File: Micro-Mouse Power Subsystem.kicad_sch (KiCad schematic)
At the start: 29 parts, among them J1 Pin Header, Q1 2N7002, Q2 AO3401A, Q3 AO3400A, Q4 AO3400A, Q5 AO3401A, U1 TP4056, U2 brushed DC motors, U3 auxiliary motors

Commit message: V1.1
- Refined Motor drivers
- Added USBC
- Added JST (don't know connections yet)
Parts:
- added C9: 1uF, Capacitor_SMD:C_0603_1608Metric, symbol Device:C
- added J2: TYPE-C-31-M-12, Connector_USB:USB_C_Receptacle_HRO_TYPE-C-31-M-12, symbol TYPE-C-31-M-12:TYPE-C-31-M-12
- added J3: Conn_01x02, Connector_JST:JST_PH_B2B-PH-K_1x02_P2.00mm_Vertical, symbol Connector_Generic:Conn_01x02
- added R9: 75K, Resistor_SMD:R_0603_1608Metric, symbol Device:R_US
- added U4: HUSB237-AA001-DN06R, Package_DFN_QFN:DFN-6-1EP_2x2mm_P0.65mm_EP1x1.6mm, symbol custom symbols:HUSB237-AA001-DN06R
- U2, U3: footprint Package_SO:HTSSOP-16-1EP_4.4x5mm_P0.65mm_EP3.4x5mm_Mask3x3mm_ThermalVias -> Package_SO:HTSSOP-16-1EP_4.4x5mm_P0.65mm_EP3.4x5mm_Mask2.46x2.31mm_ThermalVias
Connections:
- net GND: now also C9.2, J2.A1 (GND), J2.A12 (GND), J2.B1 (GND), J2.B12 (GND), J2.S1 (SHIELD), R9.2, U4.7 (GND)
- net HV (9V): now reaches J1.22 (Pin_22)
- net HV (9V): now also C9.1, J2.A4 (VBUS), J2.A9 (VBUS), J2.B4 (VBUS), J2.B9 (VBUS), U4.2 (VBUS)
- new net: J2.A5 (CC1), U4.1 (CC1)
- new net: R9.1, U4.3 (VSET)
- new net: J2.A6 (DP1), J2.B6 (DP2), U4.4 (D+)
- new net: J2.A7 (DN1), J2.B7 (DN2), U4.5 (D-)
- new net: J2.B5 (CC2), U4.6 (CC2)
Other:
- note added: "ON/OFF Switch"
- note added: "USB-C to 9V Power Output"
- note removed: "Note: ASK THE HOMIES HOW THEY GOT R_VALS **DOUBLE CHECK CONNECTIONS WITH HOMIES"
- moved on the sheet: C3, C4, C5, C6, C7, C8, R5, R6, R7, R8, U2, U3

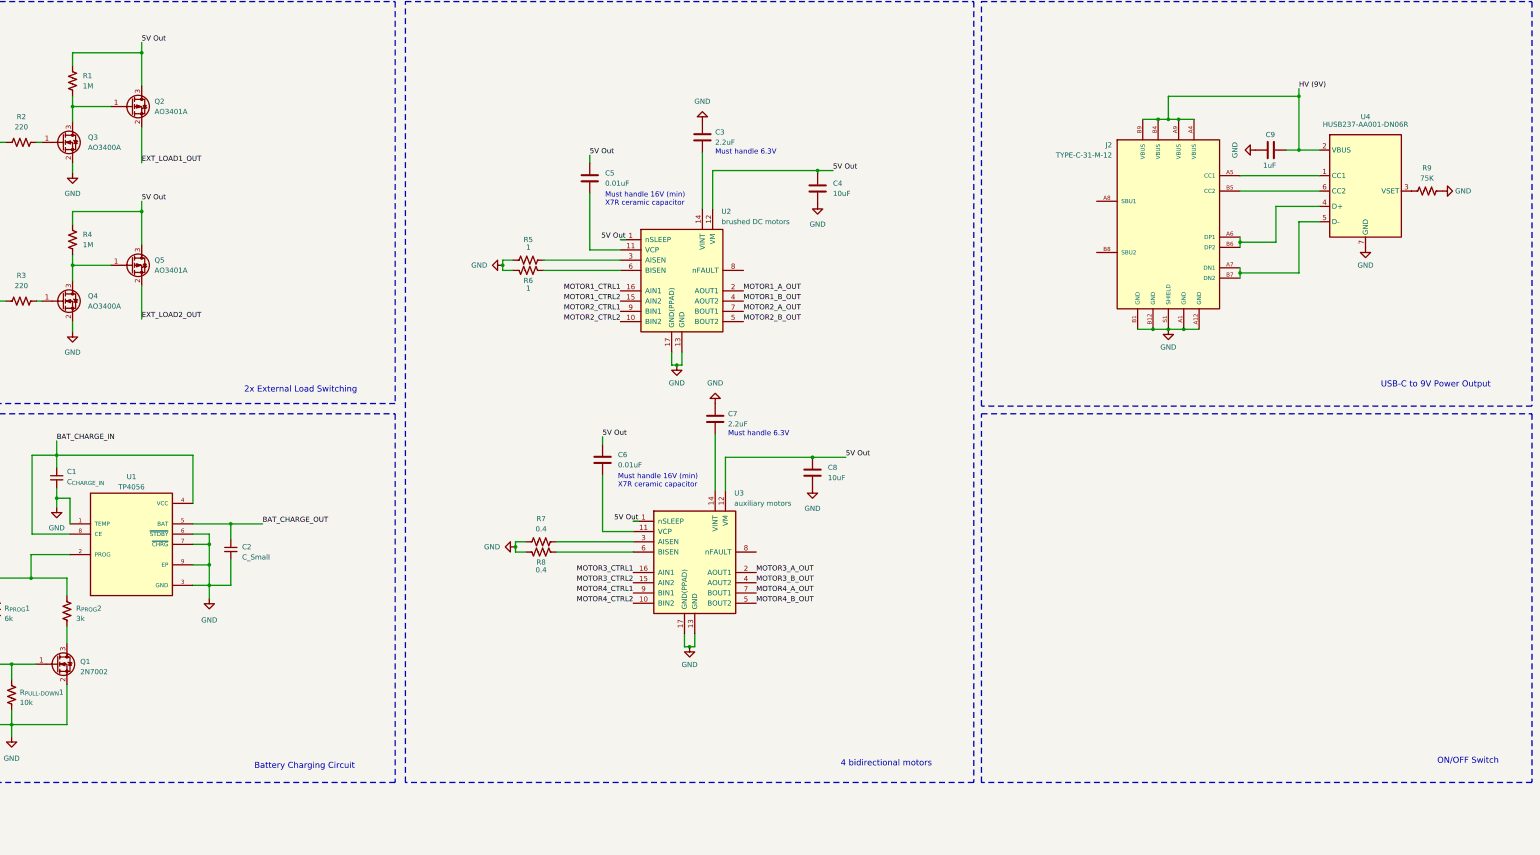
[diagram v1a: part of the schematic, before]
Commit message: still v1.1
-added switch
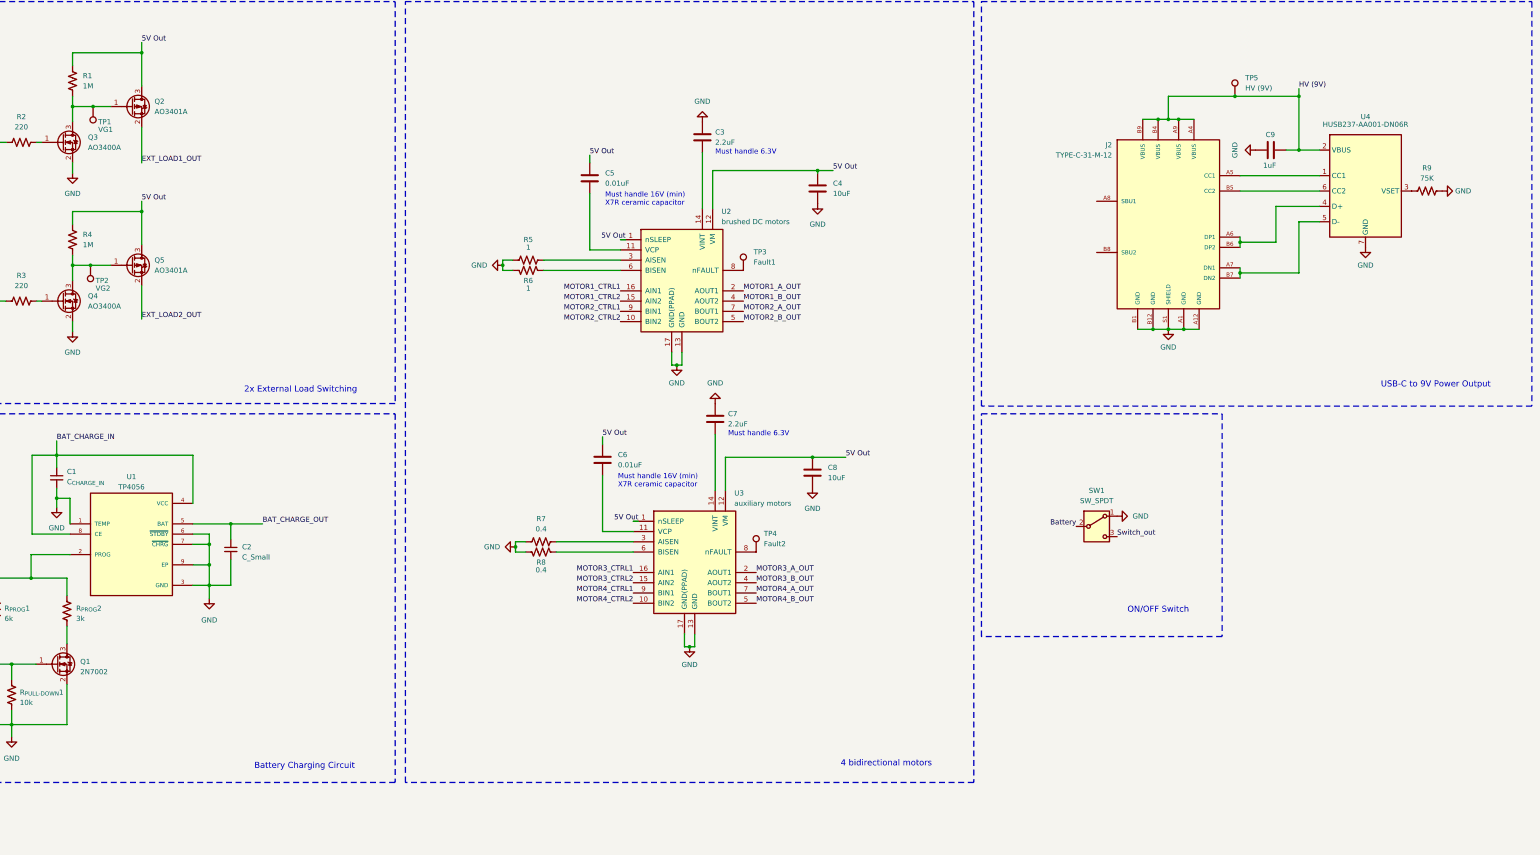
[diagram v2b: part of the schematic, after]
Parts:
- added SW1: SW_SPDT, Connector_Wire:SolderWire-0.75sqmm_1x03_P4.8mm_D1.25mm_OD2.3mm, symbol Switch:SW_SPDT
- added TP1: VG1, symbol Connector:TestPoint
- added TP2: VG2, symbol Connector:TestPoint
- added TP3: Fault1, symbol Connector:TestPoint
- added TP4: Fault2, symbol Connector:TestPoint
- added TP5: HV (9V), symbol Connector:TestPoint
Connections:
- net Battery : now also SW1.2 (B)
- net GND: now also SW1.1 (A)
- net HV (9V): now also TP5.1
- net at Q4.3 (D), Q5.1 (G), R4.2: now also TP2.1
- net at U2.8 (nFAULT): now also TP3.1
- net at U3.8 (nFAULT): now also TP4.1
- net at Q2.1 (G), Q3.3 (D), R1.2: now also TP1.1
- new net Switch_out: SW1.3 (C)
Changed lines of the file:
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@@
   (junction (at 341.63 93.98) (diameter 0) (color 0 0 0 0)
   )
+  (junction (at 78.105 78.105) (diameter 0) (color 0 0 0 0)
+  )
+  (junction (at 78.74 38.735) (diameter 0) (color 0 0 0 0)
+  )
+  (junction (at 361.95 36.195) (diameter 0) (color 0 0 0 0)
+  )
   (junction (at 58.547 177.038) (diameter 0) (color 0 0 0 0)
   )
@@
     (stroke (width 0) (type default))
   )
+  (wire (pts (xy 361.95 36.195) (xy 345.44 36.195))
+    (stroke (width 0) (type default))
+  )
   (wire (pts (xy 64.77 47.625) (xy 66.04 47.625))
     (stroke (width 0) (type default))
@@
     (stroke (width 0) (type default))
   )
+  (wire (pts (xy 78.74 38.735) (xy 83.185 38.735))
+    (stroke (width 0) (type default))
+  )
   (wire (pts (xy 53.975 47.625) (xy 57.15 47.625))
     (stroke (width 0) (type default))
@@
     (stroke (width 0) (type default))
   )
-  (wire (pts (xy 377.825 36.195) (xy 345.44 36.195))
+  (wire (pts (xy 377.825 36.195) (xy 361.95 36.195))
     (stroke (width 0) (type default))
   )
@@
     (stroke (width 0) (type default))
   )
+  (wire (pts (xy 78.105 78.105) (xy 83.185 78.105))
+    (stroke (width 0) (type default))
+  )
   (wire (pts (xy 363.22 80.01) (xy 363.22 81.28))
     (stroke (width 0) (type default))
@@
     (stroke (width 0) (type default))
   )
-  (wire (pts (xy 73.66 78.105) (xy 83.185 78.105))
+  (wire (pts (xy 73.66 78.105) (xy 78.105 78.105))
     (stroke (width 0) (type default))
   )
@@
     (stroke (width 0) (type default))
   )
-  (wire (pts (xy 73.66 38.735) (xy 83.185 38.735))
+  (wire (pts (xy 73.66 38.735) (xy 78.74 38.735))
     (stroke (width 0) (type default))
   )
@@
     (fill (type none))
   )
-  (rectangle (start 299.085 114.935) (end 435.61 206.375)
+  (rectangle (start 299.085 114.935) (end 358.775 170.18)
     (stroke (width 0) (type dash) (color 0 0 0 1))
     (fill (type none))
@@
     (effects (font (size 1.5 1.5) (color 0 0 0 1)) (justify left bottom))
   )
-  (text "ON/OFF Switch" (at 412.115 201.93 0)
+  (text "ON/OFF Switch" (at 335.28 164.465 0)
     (effects (font (size 1.5 1.5) (color 0 0 0 1)) (justify left bottom))
   )
@@
     (effects (font (size 1.27 1.27)) (justify right bottom))
   )
+  (label "Battery " (at 322.58 142.875 180) (fields_autoplaced)
+    (effects (font (size 1.27 1.27)) (justify right bottom))
+  )
   (label "MOTOR1_CTRL1" (at 55.245 382.905 0) (fields_autoplaced)
     (effects (font (size 1.27 1.27)) (justify left bottom))
@@
   )
   (label "3V3 Out " (at 55.245 370.205 0) (fields_autoplaced)
+    (effects (font (size 1.27 1.27)) (justify left bottom))
+  )
+  (label "Switch_out" (at 332.74 145.415 0) (fields_autoplaced)
     (effects (font (size 1.27 1.27)) (justify left bottom))
   )
@@
     )
   )
+  (symbol (lib_id "Connector:TestPoint") (at 361.95 36.195 0) (unit 1)
+    (in_bom yes) (on_board yes) (dnp no) (fields_autoplaced)
+    (property "Reference" "TP5" (at 364.49 31.623 0)
+      (effects (font (size 1.27 1.27)) (justify left))
+    )
+    (property "Value" "HV (9V)" (at 364.49 34.163 0)
+      (effects (font (size 1.27 1.27)) (justify left))
+    )
+    (property "Footprint" "" (at 367.03 36.195 0)
+      (effects (font (size 1.27 1.27)) hide)
+    )
+    (property "Datasheet" "~" (at 367.03 36.195 0)
+      (effects (font (size 1.27 1.27)) hide)
+    )
+    (pin "1")
+    (instances
+      (project "Micro-Mouse Power Subsystem"
+        (path "/b84c8230-4cbd-48ad-931b-8b6e428e7801"
+          (reference "TP5") (unit 1)
+        )
+      )
+    )
+  )
   (symbol (lib_id "Device:R_US") (at 409.575 59.69 90) (unit 1)
     (in_bom yes) (on_board yes) (dnp no) (fields_autoplaced)
@@
         (path "/b84c8230-4cbd-48ad-931b-8b6e428e7801"
           (reference "C4") (unit 1)
+        )
+      )
+    )
+  )
+  (symbol (lib_id "Connector:TestPoint") (at 240.03 79.375 0) (unit 1)
+    (in_bom yes) (on_board yes) (dnp no) (fields_autoplaced)
+    (property "Reference" "TP3" (at 242.57 74.803 0)
+      (effects (font (size 1.27 1.27)) (justify left))
+    )
+    (property "Value" "Fault1" (at 242.57 77.343 0)
+      (effects (font (size 1.27 1.27)) (justify left))
+    )
+    (property "Footprint" "" (at 245.11 79.375 0)
+      (effects (font (size 1.27 1.27)) hide)
+    )
+    (property "Datasheet" "~" (at 245.11 79.375 0)
+      (effects (font (size 1.27 1.27)) hide)
+    )
+    (pin "1")
+    (instances
+      (project "Micro-Mouse Power Subsystem"
+        (path "/b84c8230-4cbd-48ad-931b-8b6e428e7801"
+          (reference "TP3") (unit 1)
         )
       )
@@
     )
   )
+  (symbol (lib_id "Connector:TestPoint") (at 243.205 149.225 0) (unit 1)
+    (in_bom yes) (on_board yes) (dnp no) (fields_autoplaced)
+    (property "Reference" "TP4" (at 245.11 144.653 0)
+      (effects (font (size 1.27 1.27)) (justify left))
+    )
+    (property "Value" "Fault2" (at 245.11 147.193 0)
+      (effects (font (size 1.27 1.27)) (justify left))
+    )
+    (property "Footprint" "" (at 248.285 149.225 0)
+      (effects (font (size 1.27 1.27)) hide)
+    )
+    (property "Datasheet" "~" (at 248.285 149.225 0)
+      (effects (font (size 1.27 1.27)) hide)
+    )
+    (pin "1")
+    (instances
+      (project "Micro-Mouse Power Subsystem"
+        (path "/b84c8230-4cbd-48ad-931b-8b6e428e7801"
+          (reference "TP4") (unit 1)
+        )
+      )
+    )
+  )
+  (symbol (lib_id "Connector:TestPoint") (at 78.74 38.735 0) (mirror x) (unit 1)
+    (in_bom yes) (on_board yes) (dnp no)
+    (property "Reference" "TP1" (at 80.01 42.545 0)
+      (effects (font (size 1.27 1.27)) (justify left))
+    )
+    (property "Value" "VG1" (at 80.01 44.45 0)
+      (effects (font (size 1.27 1.27)) (justify left))
+    )
+    (property "Footprint" "" (at 83.82 38.735 0)
+      (effects (font (size 1.27 1.27)) hide)
+    )
+    (property "Datasheet" "~" (at 83.82 38.735 0)
+      (effects (font (size 1.27 1.27)) hide)
+    )
+    (pin "1")
+    (instances
+      (project "Micro-Mouse Power Subsystem"
+        (path "/b84c8230-4cbd-48ad-931b-8b6e428e7801"
+          (reference "TP1") (unit 1)
+        )
+      )
+    )
+  )
   (symbol (lib_id "power:GND") (at 58.547 195.072 0) (unit 1)
     (in_bom yes) (on_board yes) (dnp no) (fields_autoplaced)
@@
         (path "/b84c8230-4cbd-48ad-931b-8b6e428e7801"
           (reference "#PWR010") (unit 1)
+        )
+      )
+    )
+  )
+  (symbol (lib_id "Switch:SW_SPDT") (at 327.66 142.875 0) (unit 1)
+    (in_bom yes) (on_board yes) (dnp no) (fields_autoplaced)
+    (property "Reference" "SW1" (at 327.66 133.985 0)
+      (effects (font (size 1.27 1.27)))
+    )
+    (property "Value" "SW_SPDT" (at 327.66 136.525 0)
+      (effects (font (size 1.27 1.27)))
+    )
+    (property "Footprint" "Connector_Wire:SolderWire-0.75sqmm_1x03_P4.8mm_D1.25mm_OD2.3mm" (at 327.66 142.875 0)
+      (effects (font (size 1.27 1.27)) hide)
+    )
+    (property "Datasheet" "~" (at 327.66 150.495 0)
+      (effects (font (size 1.27 1.27)) hide)
+    )
+    (pin "2")
+    (pin "3")
+    (pin "1")
+    (instances
+      (project "Micro-Mouse Power Subsystem"
+        (path "/b84c8230-4cbd-48ad-931b-8b6e428e7801"
+          (reference "SW1") (unit 1)
         )
       )
@@
     )
   )
+  (symbol (lib_id "power:GND") (at 332.74 140.335 90) (unit 1)
+    (in_bom yes) (on_board yes) (dnp no) (fields_autoplaced)
+    (property "Reference" "#PWR018" (at 339.09 140.335 0)
+      (effects (font (size 1.27 1.27)) hide)
+    )
+    (property "Value" "GND" (at 336.55 140.335 90)
+      (effects (font (size 1.27 1.27)) (justify right))
+    )
+    (property "Footprint" "" (at 332.74 140.335 0)
+      (effects (font (size 1.27 1.27)) hide)
+    )
+    (property "Datasheet" "" (at 332.74 140.335 0)
+      (effects (font (size 1.27 1.27)) hide)
+    )
+    (pin "1")
+    (instances
+      (project "Micro-Mouse Power Subsystem"
+        (path "/b84c8230-4cbd-48ad-931b-8b6e428e7801"
+          (reference "#PWR018") (unit 1)
+        )
+      )
+    )
+  )
   (symbol (lib_id "Connector_Generic:Conn_01x02") (at 132.715 366.395 0) (unit 1)
     (in_bom yes) (on_board yes) (dnp no) (fields_autoplaced)
@@
         )
       )
+    )
+  )
+  (symbol (lib_id "Connector:TestPoint") (at 78.105 78.105 0) (mirror x) (unit 1)
+    (in_bom yes) (on_board yes) (dnp no)
+    (property "Reference" "TP2" (at 79.375 81.915 0)
+      (effects (font (size 1.27 1.27)) (justify left))
+    )
+    (property "Value" "VG2" (at 79.375 83.82 0)
+      (effects (font (size 1.27 1.27)) (justify left))
+    )
+    (property "Footprint" "" (at 83.185 78.105 0)
+      (effects (font (size 1.27 1.27)) hide)
+    )
+    (property "Datasheet" "~" (at 83.185 78.105 0)
+      (effects (font (size 1.27 1.27)) hide)
+    )
+    (pin "1")
+    (instances
+      (project "Micro-Mouse Power Subsystem"
+        (path "/b84c8230-4cbd-48ad-931b-8b6e428e7801"
+          (reference "TP2") (unit 1)
+        )
+      )

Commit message: changes
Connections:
- net GND: no longer SW1.1 (A)
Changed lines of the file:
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@@
-    )
-  )
-  (symbol (lib_id "power:GND") (at 332.74 140.335 90) (unit 1)
-    (in_bom yes) (on_board yes) (dnp no) (fields_autoplaced)
-    (property "Reference" "#PWR018" (at 339.09 140.335 0)
-      (effects (font (size 1.27 1.27)) hide)
-    )
-    (property "Value" "GND" (at 336.55 140.335 90)
-      (effects (font (size 1.27 1.27)) (justify right))
-    )
-    (property "Footprint" "" (at 332.74 140.335 0)
-      (effects (font (size 1.27 1.27)) hide)
-    )
-    (property "Datasheet" "" (at 332.74 140.335 0)
-      (effects (font (size 1.27 1.27)) hide)
-    )
-    (pin "1")
-    (instances
-      (project "Micro-Mouse Power Subsystem"
-        (path "/b84c8230-4cbd-48ad-931b-8b6e428e7801"
-          (reference "#PWR018") (unit 1)
-        )
-      )
     )
   )

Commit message: Update to KiCad 9.0
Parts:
- J3: footprint Connector_JST:JST_PH_B2B-PH-K_1x02_P2.00mm_Vertical -> Connector_JST:JST_PH_S2B-PH-K_1x02_P2.00mm_Horizontal
- TP1, TP2, TP3, TP4, TP5: footprint (none) -> TestPoint:TestPoint_Pad_1.5x1.5mm
- U2: value brushed DC motors -> brushed DC motors
- U3: value auxiliary motors -> auxiliary motors

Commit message: V2
- all schematics are uploaded
- missing a few footprints from Sinaye
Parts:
- removed C1: C_{CHARGE_IN}, Capacitor_SMD:C_0603_1608Metric, symbol Device:C_Small
- removed C2: C_Small, Capacitor_SMD:C_0603_1608Metric, symbol Device:C_Small
- removed R_{PULL-DOWN}1: 10k, Resistor_SMD:R_0603_1608Metric, symbol Device:R_US
- removed U1: TP4056, TP4056:SOP127P600X175-9N, symbol TP4056:TP4056
- added C10, C_{1}1: 1uF, symbol Device:C_Small
- added C_{BOOT}1, C_{BY}1: 0.1uF, symbol Device:C_Small
- added C_{BYPASS}1: 0.1u, symbol Device:C_Small
- added C_{CHARGE_IN}1, C_{CHARGE_OUT}1: 10u, symbol Device:C_Small
- added C_{COMP}1: 1nF, symbol Device:C_Small
- added C_{IN_3.3}1, C_{IN_3.3}2, C_{IN}1, C_{IN}2, C_{OUT_3.3}1, C_{OUT_3.3}2, C_{OUT_3.3}3, C_{OUT}1, C_{OUT}2, C_{OUT}3: 100uF, symbol Device:C_Small
- added C_{IN_3.3}3, C_{IN}3, C_{OUT}4, C_{OUT}5, C_{OUT}6: 22uF, symbol Device:C_Small
- added C_{IN_5}1: 10uF, symbol Device:C_Small
- added C_{SS}1: 47nF, symbol Device:C_Small
- added D3, D4: SK32WA, symbol Device:D_Schottky
- added L1: L, symbol Device:L
- added L2, L4: 22uH, symbol Device:L
- added R_{COMP}1: 68k, symbol Device:R_US
- added R_{FB}1: 150k, symbol Device:R_US
- added R_{FB}2: 47k, symbol Device:R_US
- added R_{FSW}1: 220k, symbol Device:R_US
- added R_{FSW}2: 33k, symbol Device:R_US
- added R_{ILIM}1: 100k, symbol Device:R_US
- added R_{PULL_DOWN}1: 10k, symbol Device:R_US
- added R_{SCL}1, R_{SDA}1: 4.7k, symbol Device:R_US
- added R_{SHUNT}1: 0.05, symbol Device:R_US
- added U1: TP4056-42-ESOP8, Package_SO:SOIC-8-1EP_3.9x4.9mm_P1.27mm_EP2.41x3.3mm_ThermalVias, symbol Battery_Management:TP4056-42-ESOP8
- added U5: TPS61088RHLR, TPS61088RHLR:IC_TPS61088RHLR, symbol TPS61088RHLR:TPS61088RHLR
- added U6: INA219AIDCNR, INA219AIDCNR:SOT65P280X145-8N, symbol INA219AIDCNR:INA219AIDCNR
- added U7: XL1509-3.3, Package_SO:SOIC-8_3.9x4.9mm_P1.27mm, symbol Regulator_Switching:XL1509-3.3
- added U8: XL1509-5.0, Package_SO:SOIC-8_3.9x4.9mm_P1.27mm, symbol Regulator_Switching:XL1509-5.0
- R_{LIMIT}1: footprint Resistor_SMD:R_0603_1608Metric -> (none)
- R_{PROG}1: value 6k -> 5.6k; footprint Resistor_SMD:R_0603_1608Metric -> (none)
- R_{PROG}2: value 3k -> 2.7k; footprint Resistor_SMD:R_0603_1608Metric -> (none)
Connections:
- net GND: now also C_{BY}1.2, C_{CHARGE_IN}1.2, C_{CHARGE_OUT}1.2, C_{COMP}1.2, C_{IN_5}1.1, C_{OUT}4.2, C_{OUT}5.2, C_{OUT}6.2, C_{SS}1.2, R_{FB}2.1, R_{ILIM}1.2, R_{PULL_DOWN}1.2, U1.1 (TEMP), U1.3 (GND), U1.6 (~{STDBY}), U1.7 (~{CHRG}), U1.9 (EPAD), U5.1 (VCC), U5.20 (AGND), U5.21 (PGND), U5.22 (PGND), U5.23 (PGND), U5.24 (PGND), U5.25 (PGND), U5.26 (PGND), U5.27 (PGND), U5.28 (PGND), U5.29 (PGND), U6.3 (GND), U6.7 (A0)
- net at R_{PROG}1.1, R_{PROG}2.1: now also U1.2 (PROG)
- net at Q1.1 (G), R_{LIMIT}1.2: now also R_{PULL_DOWN}1.1
- net FAST_CHARGE_OUT renamed FAST_CHARGE_CTRL
- new net: R_{SHUNT}1.1, U6.2 (IN-)
- new net: C_{1}1.2, C_{IN}1.2, C_{IN}2.2, C_{IN}3.2, C_{OUT}1.2, C_{OUT}2.2, C_{OUT}3.2, D4.2 (A), U8.4 (~{EN}), U8.5 (GND), U8.6 (GND), U8.7 (GND), U8.8 (GND)
- new net: C10.2, C_{IN_3.3}1.2, C_{IN_3.3}2.2, C_{IN_3.3}3.2, C_{OUT_3.3}1.2, C_{OUT_3.3}2.2, C_{OUT_3.3}3.2, D3.2 (A), U7.4 (~{EN}), U7.5 (GND), U7.6 (GND), U7.7 (GND), U7.8 (GND)
- new net: D4.1 (K), L4.1, U8.2 (OUT)
- new net: C_{SS}1.1, U5.10 (SS)
- new net: R_{COMP}1.1, U5.18 (COMP)
- new net: R_{ILIM}1.1, U5.19 (ILIM)
- new net: R_{FSW}2.2, U5.3 (FSW)
- new net: C_{BOOT}1.1, U5.8 (BOOT)
- new net: C_{CHARGE_IN}1.1, U1.4 (V_{CC}), U1.8 (CE)
- new net: C_{CHARGE_OUT}1.1, U1.5 (BAT)
- new net: R_{SCL}1.1, U6.5 (SCL)
- new net: D3.1 (K), L2.1, U7.2 (OUT)
- new net: C_{BYPASS}1.1, U6.4 (VS)
- new net: R_{SDA}1.2, U6.6 (SDA)
- new net: R_{FSW}1.2, R_{FSW}2.1
- new net: C_{COMP}1.1, R_{COMP}1.2
- new net 3.3V_OUT: C_{OUT_3.3}1.1, C_{OUT_3.3}2.1, C_{OUT_3.3}3.1, L2.2, U7.3 (FB)
- new net 3V3_OUT: C_{BYPASS}1.2, U6.8 (A1)
- new net 5V_BAT_CHARGE: C_{OUT}1.1, C_{OUT}2.1, C_{OUT}3.1, L4.2, U8.3 (FB)
- new net 5V_OUT: C10.1, C_{IN_3.3}1.1, C_{IN_3.3}2.1, C_{IN_3.3}3.1, C_{OUT}4.1, C_{OUT}5.1, C_{OUT}6.1, R_{FB}1.2, U5.15 (VOUT_14), U7.1 (VIN)
- new net 9V_INPUT: C_{1}1.1, C_{IN}1.1, C_{IN}2.1, C_{IN}3.1, U8.1 (VIN)
- new net BATTERY+: C_{BY}1.1, C_{IN_5}1.2, L1.1, R_{SHUNT}1.2, U5.2 (EN), U5.9 (VIN), U6.1 (IN+)
- new net BOOT: C_{BOOT}1.2, L1.2, R_{FSW}1.1, U5.5 (SW_4)
- new net FB: R_{FB}1.1, R_{FB}2.2, U5.17 (FB)
- new net I2C1_SCL: R_{SCL}1.2
- new net I2C1_SDA: R_{SDA}1.1
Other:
- note added: "9V Input Step-Down"
- note added: "Battery Monitoring Circuit"
- note added: "Voltage Regulation"
- moved on the sheet: J1, J3, SW1
